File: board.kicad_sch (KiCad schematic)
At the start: 47 parts, among them J1 TEMPS, J2 OLED, J3 HV1, J4 HV2, J5 PWR_IN, J6 PROG, K1 RELAY1, K3 RELAY2, Q3 AO3400A, Q4 AO3400A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

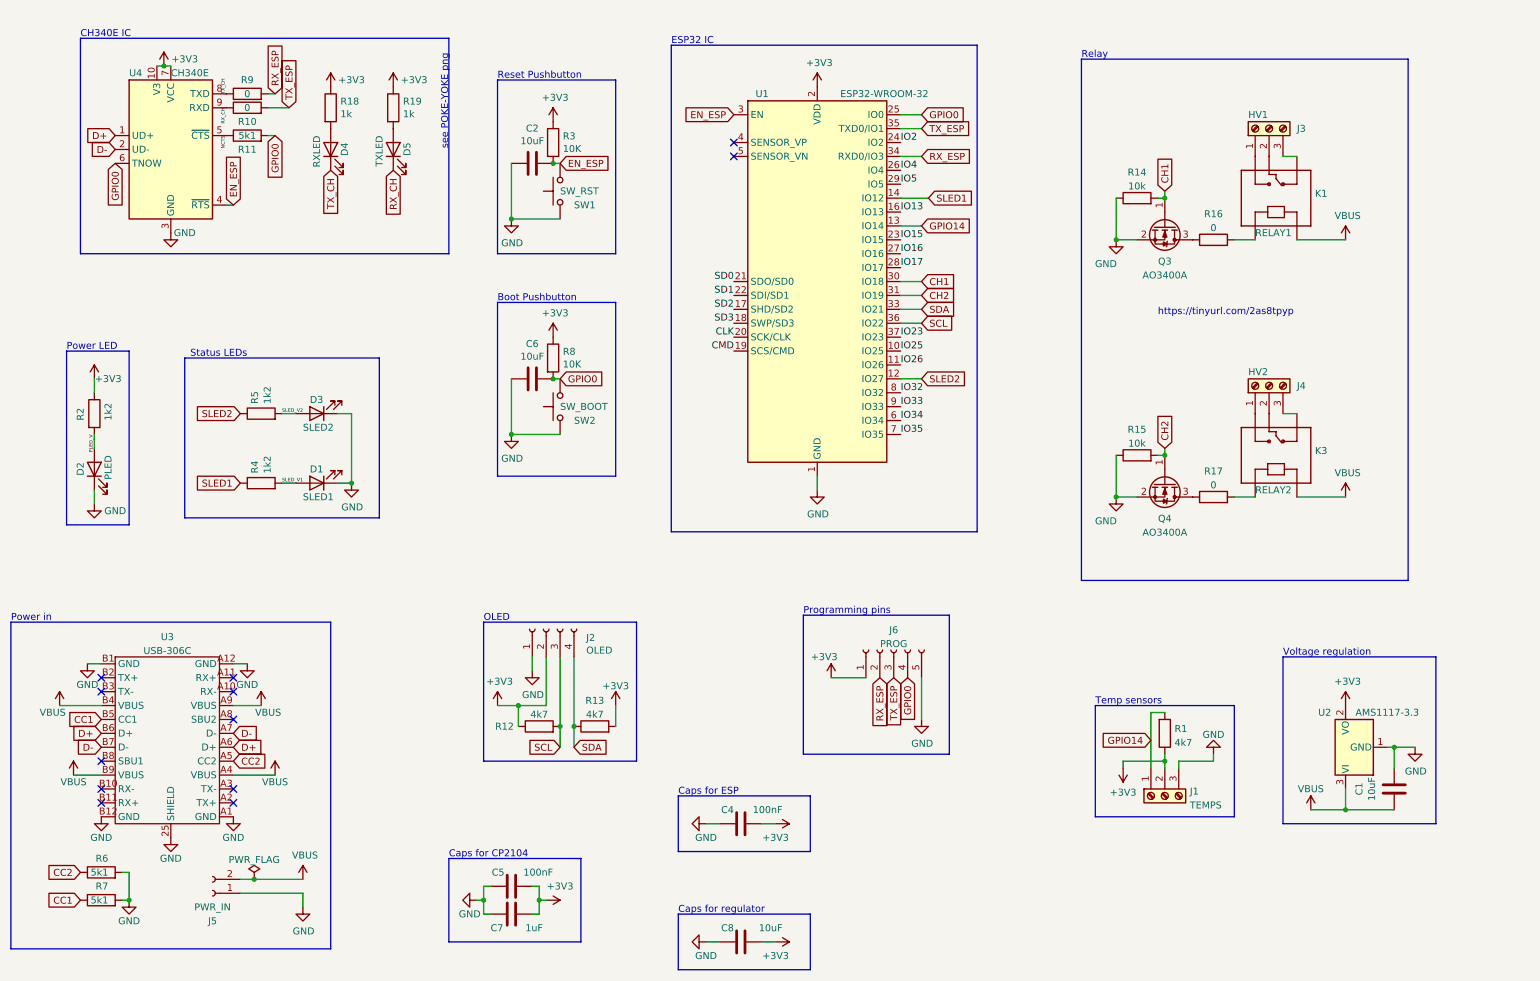
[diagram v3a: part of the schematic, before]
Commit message: feat: redesigned board for 5x5
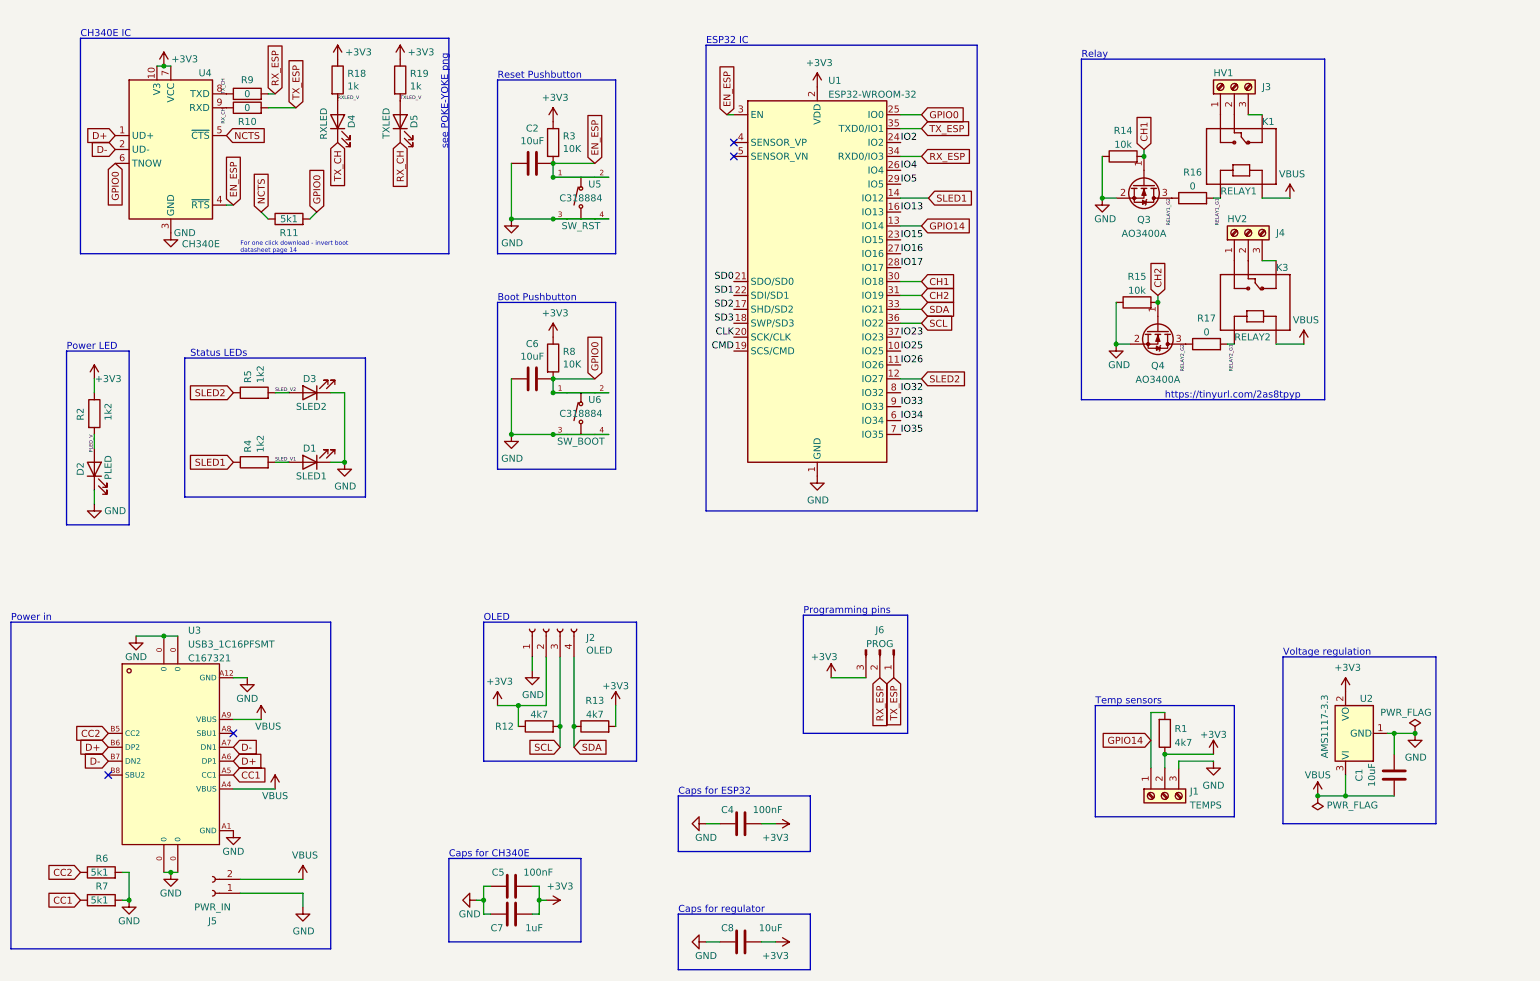
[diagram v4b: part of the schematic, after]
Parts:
- removed J6: PROG, Connector_PinHeader_2.54mm:PinHeader_1x05_P2.54mm_Vertical, symbol Connector:Conn_01x05_Female
- removed K1: RELAY1, SRD-05VDC-SL-C:RELAY_SRD-05VDC-SL-C, symbol SRD-05VDC-SL-C:SRD-05VDC-SL-C
- removed K3: RELAY2, SRD-05VDC-SL-C:RELAY_SRD-05VDC-SL-C, symbol SRD-05VDC-SL-C:SRD-05VDC-SL-C
- removed SW1: SW_RST, Button_Switch_THT:SW_PUSH_6mm_H4.3mm, symbol Switch:SW_Push
- removed SW2: SW_BOOT, Button_Switch_THT:SW_PUSH_6mm_H4.3mm, symbol Switch:SW_Push
- removed U1: ESP32-WROOM-32, RF_Module:ESP32-WROOM-32, symbol RF_Module:ESP32-WROOM-32
- removed U3: USB-306C, board:USB-TYPE-C-TH_USB-306C, symbol board:USB-306C
- removed U4: CH340E, Package_SO:MSOP-10_3x3mm_P0.5mm, symbol Interface_USB:CH340E
- added J6: PROG, Connector_PinHeader_2.54mm:PinHeader_1x03_P2.54mm_Vertical, symbol Connector:Conn_01x03_Male
- added K1: RELAY1, board:RELAY_SRD-05VDC-SL-C, symbol board:SRD-05VDC-SL-C
- added K3: RELAY2, board:RELAY_SRD-05VDC-SL-C, symbol board:SRD-05VDC-SL-C
- added U1: ESP32-WROOM-32, RF_Module:ESP32-WROOM-32, symbol board:ESP32-WROOM-32
- added U3: USB3_1C16PFSMT, board:USB-C-SMD_TYPE-C-USB-17, symbol board:USB3_1C16PFSMT
- added U4: CH340E, Package_SO:MSOP-10_3x3mm_P0.5mm, symbol board:CH340E
- added U5: SW_RST, board:SW-SMD_4P-L5.1-W5.1-P3.70-LS6.5-TL-2, symbol board:TS-1187A-B-A-B
- added U6: SW_BOOT, board:SW-SMD_4P-L5.1-W5.1-P3.70-LS6.5-TL-2, symbol board:TS-1187A-B-A-B
- C1, C2, C4, C5, C6, C7, C8: footprint Capacitor_SMD:C_0805_2012Metric -> Capacitor_SMD:C_0603_1608Metric
- R1, R10, R11, R12, R13, R14, R15, R16, R17, R18, R19, R2, R3, R4, R5, R6, R7, R8, R9: footprint Resistor_SMD:R_0805_2012Metric -> Resistor_SMD:R_0603_1608Metric
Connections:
- net +3V3: now also J6.3 (Pin_3), U1.2 (VDD), U4.10 (V3), U4.7 (VCC)
- net CC1: now also U3.A5 (CC1)
- net CC2: now also U3.B5 (CC2)
- net CH1: now also U1.30 (IO18)
- net CH2: now also U1.31 (IO19)
- net CLK: now also U1.20 (SCK/CLK)
- net CMD: now also U1.19 (SCS/CMD)
- net D+: now also U3.A6 (DP1), U3.B6 (DP2), U4.1 (UD+)
- net D-: now also U3.A7 (DN1), U3.B7 (DN2), U4.2 (UD-)
- net EN_ESP: now also U1.3 (EN), U4.4 (~{RTS}), U5.1 (A), U5.2 (B)
- net GND: now also U1.1 (GND), U1.15 (GND), U1.38 (GND), U1.39 (GND), U3.0, U3.A1 (GND), U3.A12 (GND), U4.3 (GND), U5.3 (C), U5.4 (D), U6.3 (C), U6.4 (D)
- net GPIO0: now also U1.25 (IO0), U4.6 (TNOW), U6.1 (A), U6.2 (B)
- net GPIO14: now also U1.13 (IO14)
- net IO13: now also U1.16 (IO13)
- net IO15: now also U1.23 (IO15)
- net IO16: now also U1.27 (IO16)
- net IO17: now also U1.28 (IO17)
- net IO2: now also U1.24 (IO2)
- net IO23: now also U1.37 (IO23)
- net IO25: now also U1.10 (IO25)
- net IO26: now also U1.11 (IO26)
- net IO32: now also U1.8 (IO32)
- net IO33: now also U1.9 (IO33)
- net IO34: now also U1.6 (IO34)
- net IO35: now also U1.7 (IO35)
- net IO4: now also U1.26 (IO4)
- net IO5: now also U1.29 (IO5)
- net NCTS: now also U4.5 (~{CTS})
- net RX_CH: now also U4.9 (RXD)
- net RX_ESP: now also J6.2 (Pin_2), U1.34 (RXD0/IO3)
- net SCL: now also U1.36 (IO22)
- net SD0: now also U1.21 (SDO/SD0)
- net SD1: now also U1.22 (SDI/SD1)
- net SD2: now also U1.17 (SHD/SD2)
- net SD3: now also U1.18 (SWP/SD3)
- net SDA: now also U1.33 (IO21)
- net SLED1: now also U1.14 (IO12)
- net SLED2: now also U1.12 (IO27)
- net TX_CH: now also U4.8 (TXD)
- net TX_ESP: now also J6.1 (Pin_1), U1.35 (TXD0/IO1)
- net VBUS: now also K1.A2, K3.A2, U3.A4 (VBUS), U3.A9 (VBUS)
- net RELAY2_G2: now reaches Q4.3 (D), R17.1
- net RELAY2_G1: now reaches R17.2
- net RELAY2_G1: now also K3.A1
- net RELAY1_G2: now reaches Q3.3 (D), R16.1
- net RELAY1_G1: now reaches R16.2
- net RELAY1_G1: now also K1.A1
- net TXLED_V: now reaches D5.2 (A), R19.2
- net at J4.2 (Pin_2): now also K3.COM
- net at J4.3 (Pin_3): now also K3.NC
- net at J4.1 (Pin_1): now also K3.NO
- net RXLED_V: now reaches D4.2 (A), R18.2
- net at J3.2 (Pin_2): now also K1.COM
- net at J3.3 (Pin_3): now also K1.NC
- net at J3.1 (Pin_1): now also K1.NO
- no-connect marks 12 -> 4
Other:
- note added: "Caps for CH340E"
- note added: "Caps for ESP32"
- note added: "For one click download - invert boot datasheet page 14"
- note removed: "Caps for CP2104"
- note removed: "Caps for ESP"
- moved on the sheet: C1, D1, D3, D4, D5, J3, J4, Q3, Q4, R11, R14, R15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

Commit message: feat: initial routing
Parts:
- removed U5: SW_RST, board:SW-SMD_4P-L5.1-W5.1-P3.70-LS6.5-TL-2, symbol board:TS-1187A-B-A-B
- removed U6: SW_BOOT, board:SW-SMD_4P-L5.1-W5.1-P3.70-LS6.5-TL-2, symbol board:TS-1187A-B-A-B
- added U5: SW_RST, board:SW-SMD_L6.0-W3.5-LS8.0, symbol board:Tactile_Switch_C609852
- added U6: SW_BOOT, board:SW-SMD_L6.0-W3.5-LS8.0, symbol board:Tactile_Switch_C609852
- J3: value HV1 -> HV2
- J4: value HV2 -> HV1
- K1: value RELAY1 -> RELAY2
- K3: value RELAY2 -> RELAY1
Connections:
- net CH1: now also Q4.1 (G), R15.2; no longer Q3.1 (G), R14.2
- net CH2: now also Q3.1 (G), R14.2; no longer Q4.1 (G), R15.2
- net EN_ESP: now also U5.1
- net GND: now also U5.2, U6.2
- net GPIO0: now also U6.1
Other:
- moved on the sheet: C1, C2, C4, C5, C6, C7, C8, J1, J2, J4, J6, K3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

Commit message: feat: routed with planes and no warnings or errors
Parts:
- C1, C2, C4, C5, C6, C7, C8: footprint Capacitor_SMD:C_0603_1608Metric -> Capacitor_SMD:C_0402_1005Metric
- D1, D2, D3, D4, D5: footprint LED_SMD:LED_0805_2012Metric -> LED_SMD:LED_0603_1608Metric
- R1, R10, R11, R12, R13, R14, R15, R16, R17, R18, R19, R2, R3, R4, R5, R6, R7, R8, R9: footprint Resistor_SMD:R_0603_1608Metric -> Resistor_SMD:R_0402_1005Metric
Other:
- note added: "Relays"
- note removed: "Relay"

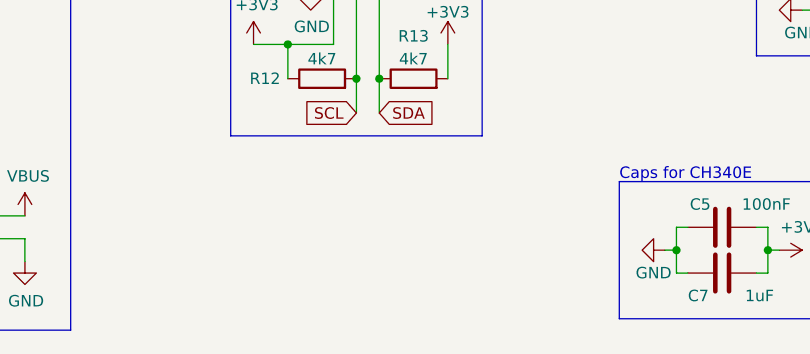
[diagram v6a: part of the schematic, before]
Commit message: chore: reorganised to respect keepout and corners
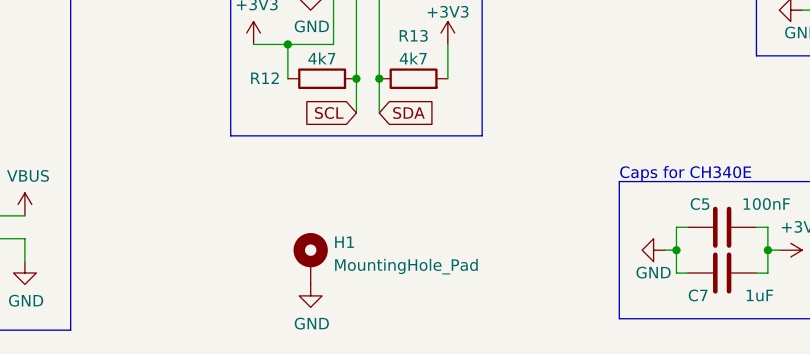
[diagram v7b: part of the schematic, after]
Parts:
- added H1: MountingHole_Pad, MountingHole:MountingHole_2.2mm_M2_DIN965_Pad, symbol Mechanical:MountingHole_Pad
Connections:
- net GND: now also H1.1
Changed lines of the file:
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@@
+    (pin "1")
+  )
+  (symbol (lib_id "power:GND") (at 105.41 180.34 0) (unit 1)
+    (in_bom yes) (on_board yes)
+    (property "Reference" "#PWR07" (id 0) (at 105.41 186.69 0)
+      (effects (font (size 1.27 1.27)) hide)
+    )
+    (property "Value" "GND" (id 1) (at 105.537 184.7342 0))
+    (property "Footprint" "" (id 2) (at 105.41 180.34 0)
+      (effects (font (size 1.27 1.27)) hide)
+    )
+    (property "Datasheet" "" (id 3) (at 105.41 180.34 0)
+      (effects (font (size 1.27 1.27)) hide)
+    )
     (pin "1")
   )
@@
     (pin "2")
     (pin "3")
+  )
+  (symbol (lib_id "Mechanical:MountingHole_Pad") (at 105.41 177.8 0) (unit 1)
+    (in_bom yes) (on_board yes) (fields_autoplaced)
+    (property "Reference" "H1" (id 0) (at 107.95 175.6953 0)
+      (effects (font (size 1.27 1.27)) (justify left))
+    )
+    (property "Value" "MountingHole_Pad" (id 1) (at 107.95 178.2322 0)
+      (effects (font (size 1.27 1.27)) (justify left))
+    )
+    (property "Footprint" "MountingHole:MountingHole_2.2mm_M2_DIN965_Pad" (id 2) (at 105.41 177.8 0)
+      (effects (font (size 1.27 1.27)) hide)
+    )
+    (property "Datasheet" "~" (id 3) (at 105.41 177.8 0)
+      (effects (font (size 1.27 1.27)) hide)
+    )
+    (pin "1")
   )
   (symbol (lib_id "power:GND") (at 49.53 54.61 0) (unit 1)
@@
       (reference "#PWR06") (unit 1) (value "GND") (footprint "")
     )
+    (path "/064e195f-e40f-4213-942e-c83b3620bd7d"
+      (reference "#PWR07") (unit 1) (value "GND") (footprint "")
+    )
     (path "/5a7f1113-6786-4953-a2be-fc9377cc6784"
       (reference "#PWR013") (unit 1) (value "GND") (footprint "")
@@
       (reference "D5") (unit 1) (value "TXLED") (footprint "LED_SMD:LED_0603_1608Metric")
     )
+    (path "/4da5a5f6-e63b-4db2-a10f-d5196783f905"
+      (reference "H1") (unit 1) (value "MountingHole_Pad") (footprint "MountingHole:MountingHole_2.2mm_M2_DIN965_Pad")
+    )
     (path "/00000000-0000-0000-0000-000060cdeb35"

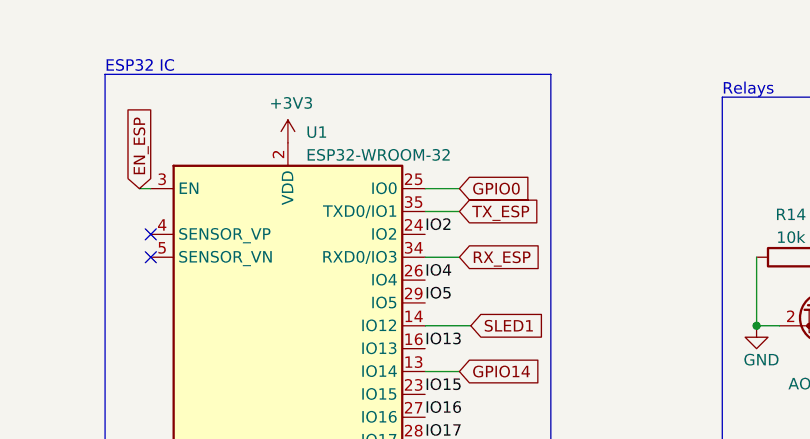
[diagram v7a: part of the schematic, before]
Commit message: chore: switched esp footprint
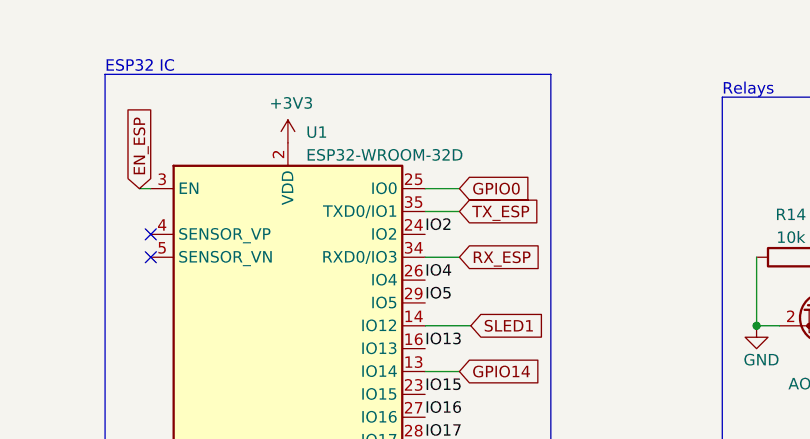
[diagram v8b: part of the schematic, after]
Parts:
- removed U1: ESP32-WROOM-32, RF_Module:ESP32-WROOM-32, symbol board:ESP32-WROOM-32
- added U1: ESP32-WROOM-32D, RF_Module:ESP32-WROOM-32, symbol RF_Module:ESP32-WROOM-32D
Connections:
- net +3V3: now also U1.2 (VDD)
- net CH1: now also U1.30 (IO18)
- net CH2: now also U1.31 (IO19)
- net CLK: now also U1.20 (SCK/CLK)
- net CMD: now also U1.19 (SCS/CMD)
- net EN_ESP: now also U1.3 (EN)
- net GND: now also U1.1 (GND), U1.15 (GND), U1.38 (GND), U1.39 (GND)
- net GPIO0: now also U1.25 (IO0)
- net GPIO14: now also U1.13 (IO14)
- net IO13: now also U1.16 (IO13)
- net IO15: now also U1.23 (IO15)
- net IO16: now also U1.27 (IO16)
- net IO17: now also U1.28 (IO17)
- net IO2: now also U1.24 (IO2)
- net IO23: now also U1.37 (IO23)
- net IO25: now also U1.10 (IO25)
- net IO26: now also U1.11 (IO26)
- net IO32: now also U1.8 (IO32)
- net IO33: now also U1.9 (IO33)
- net IO34: now also U1.6 (IO34)
- net IO35: now also U1.7 (IO35)
- net IO4: now also U1.26 (IO4)
- net IO5: now also U1.29 (IO5)
- net RX_ESP: now also U1.34 (RXD0/IO3)
- net SCL: now also U1.36 (IO22)
- net SD0: now also U1.21 (SDO/SD0)
- net SD1: now also U1.22 (SDI/SD1)
- net SD2: now also U1.17 (SHD/SD2)
- net SD3: now also U1.18 (SWP/SD3)
- net SDA: now also U1.33 (IO21)
- net SLED1: now also U1.14 (IO12)
- net SLED2: now also U1.12 (IO27)
- net TX_ESP: now also U1.35 (TXD0/IO1)
